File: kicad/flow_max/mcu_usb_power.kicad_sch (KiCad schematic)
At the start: 1 part, among them U5 MCXN947VDFT

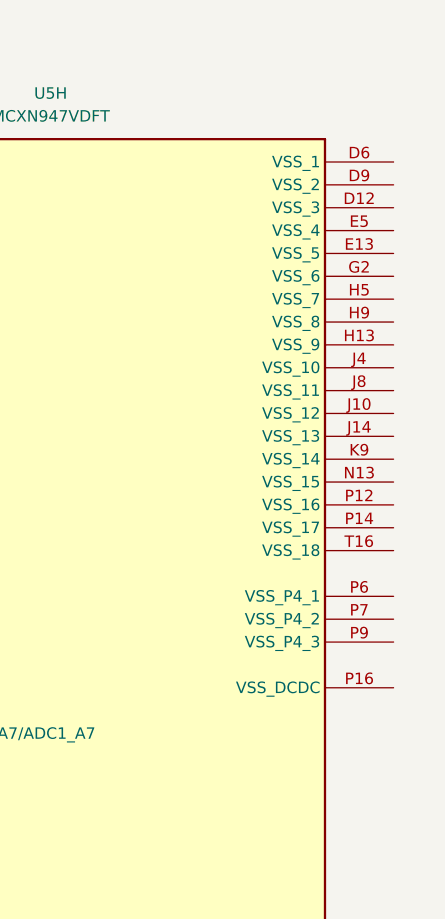
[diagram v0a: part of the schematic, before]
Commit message: Added pin assignment to MCXN947 for the communication lines, Debugger, ISP_Mode and optional GPIO/SD card
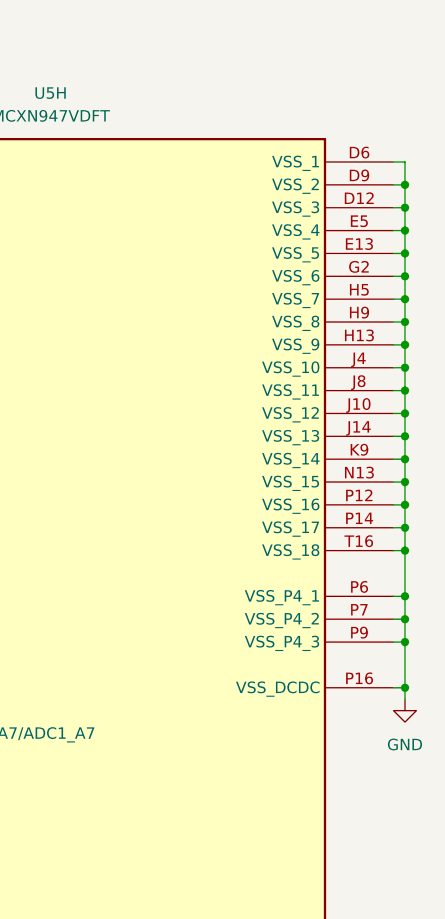
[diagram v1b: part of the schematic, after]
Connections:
- net GND: now reaches U5.D12 (VSS_3)
- net GND: now also U5.D6 (VSS_1), U5.D9 (VSS_2), U5.E13 (VSS_5), U5.E5 (VSS_4), U5.G2 (VSS_6), U5.H13 (VSS_9), U5.H5 (VSS_7), U5.H9 (VSS_8), U5.J10 (VSS_12), U5.J14 (VSS_13), U5.J4 (VSS_10), U5.J8 (VSS_11), U5.K9 (VSS_14), U5.N13 (VSS_15), U5.P12 (VSS_16), U5.P14 (VSS_17), U5.P16 (VSS_DCDC), U5.P6 (VSS_P4_1), U5.P7 (VSS_P4_2), U5.P9 (VSS_P4_3), U5.T16 (VSS_18)

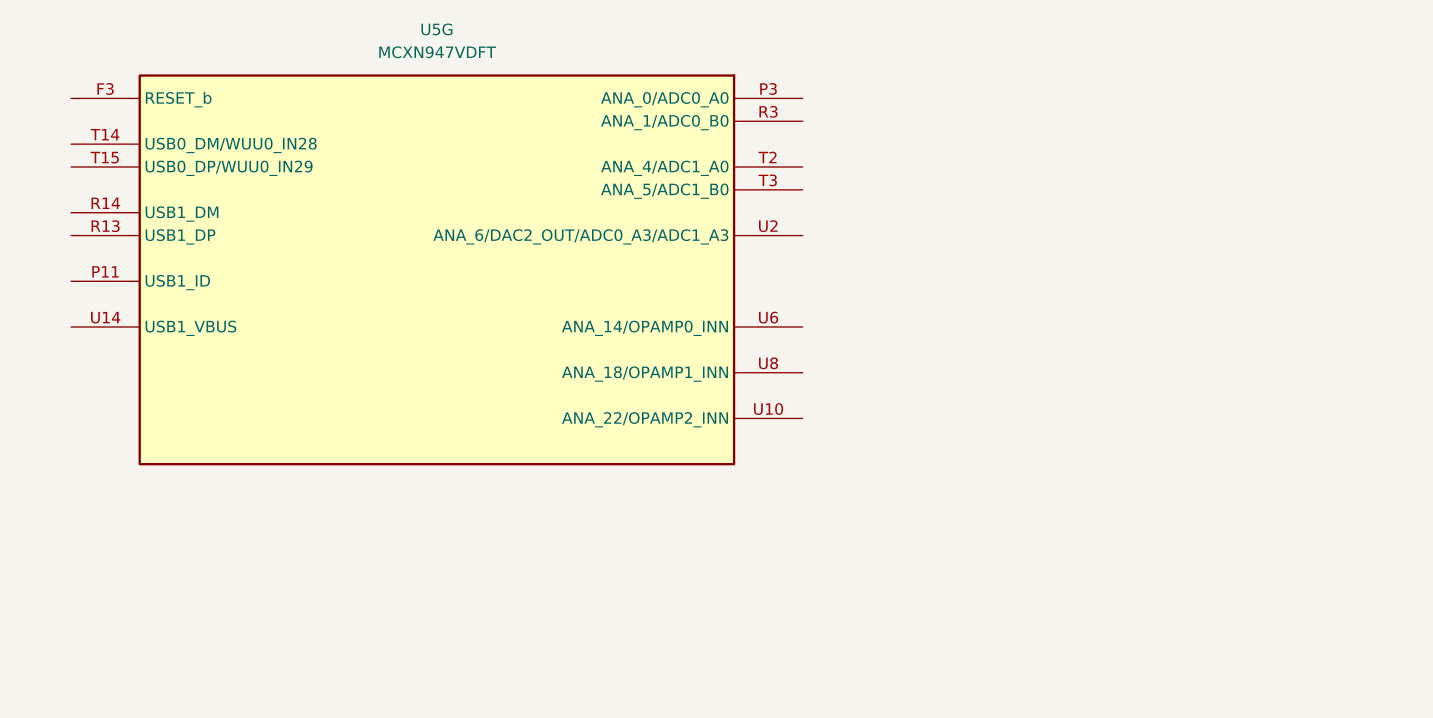
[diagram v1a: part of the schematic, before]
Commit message: Added in the schematic common mode choke filters and TVS diodes to parts where it is needed. Made the polarity protection circuit in schematic. Put placeholders for power supply regulators in schematic.
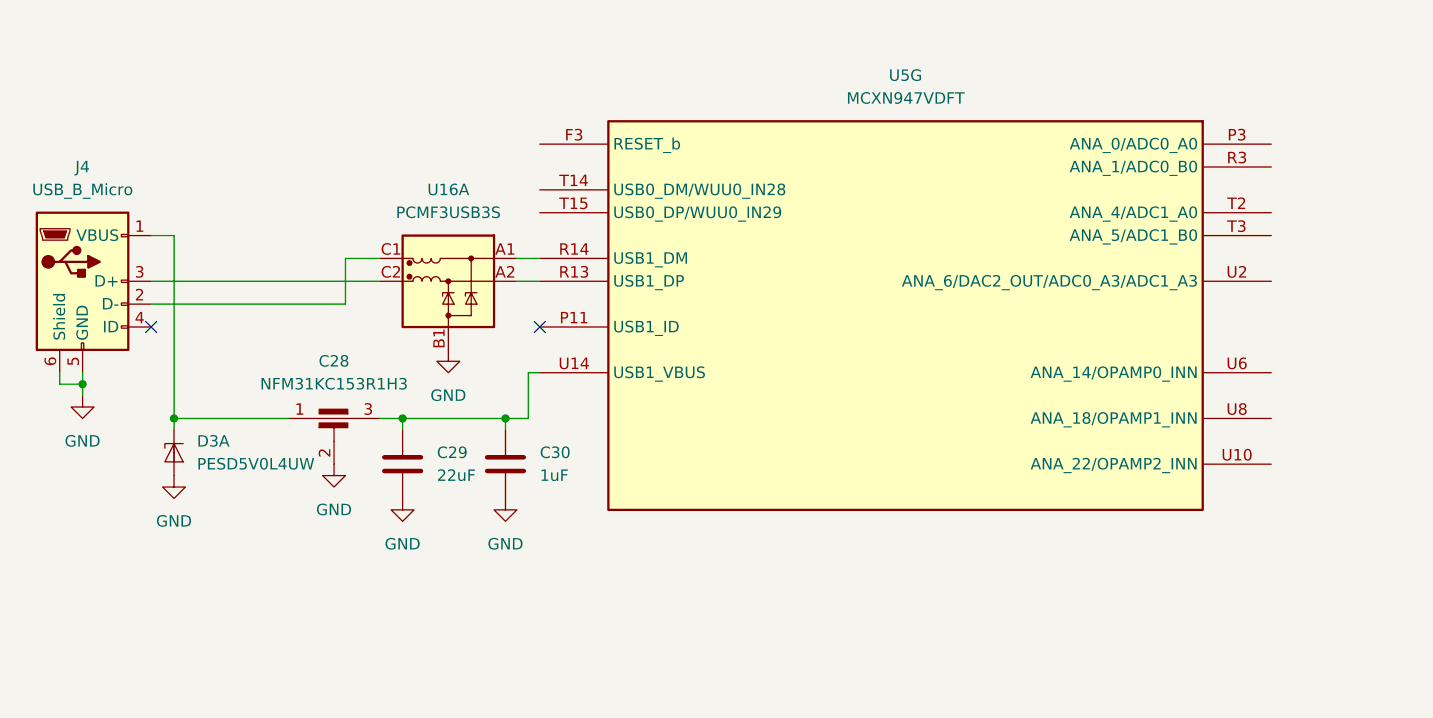
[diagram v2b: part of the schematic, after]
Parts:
- added C28: NFM31KC153R1H3, symbol Device:C_Feedthrough
- added C29: 22uF, symbol Device:C
- added C30: 1uF, symbol Device:C
- added D3: PESD5V0L4UW, Package_TO_SOT_SMD:SOT-665, symbol Power_Protection:PESD5V0L4UW
- added J4: USB_B_Micro, symbol Connector:USB_B_Micro
- added U16: PCMF3USB3S, Package_CSP:Nexperia_WLCSP-15_6-3-6_2.37x1.17mm_Layout6x3_P0.4mm, symbol Power_Protection:PCMF3USB3S
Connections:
- net GND: now also C28.2, C29.2, C30.2, D3.2 (A), J4.5 (GND), J4.6 (Shield), U16.B1 (GND_CH1)
- net at U5.R13 (USB1_DP): now also U16.A2 (CH1_IN-)
- net at U5.R14 (USB1_DM): now also U16.A1 (CH1_IN+)
- net at U5.U14 (USB1_VBUS): now also C28.3, C29.1, C30.1
- new net: C28.1, D3.1 (K1), J4.1 (VBUS)
- new net: J4.2 (D-), U16.C1 (CH1_OUT+)
- new net: J4.3 (D+), U16.C2 (CH1_OUT-)
- no-connect marks 0 -> 2
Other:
- moved on the sheet: U5G
